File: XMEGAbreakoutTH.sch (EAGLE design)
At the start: 23 parts, among them IC1 XMEGA16A4

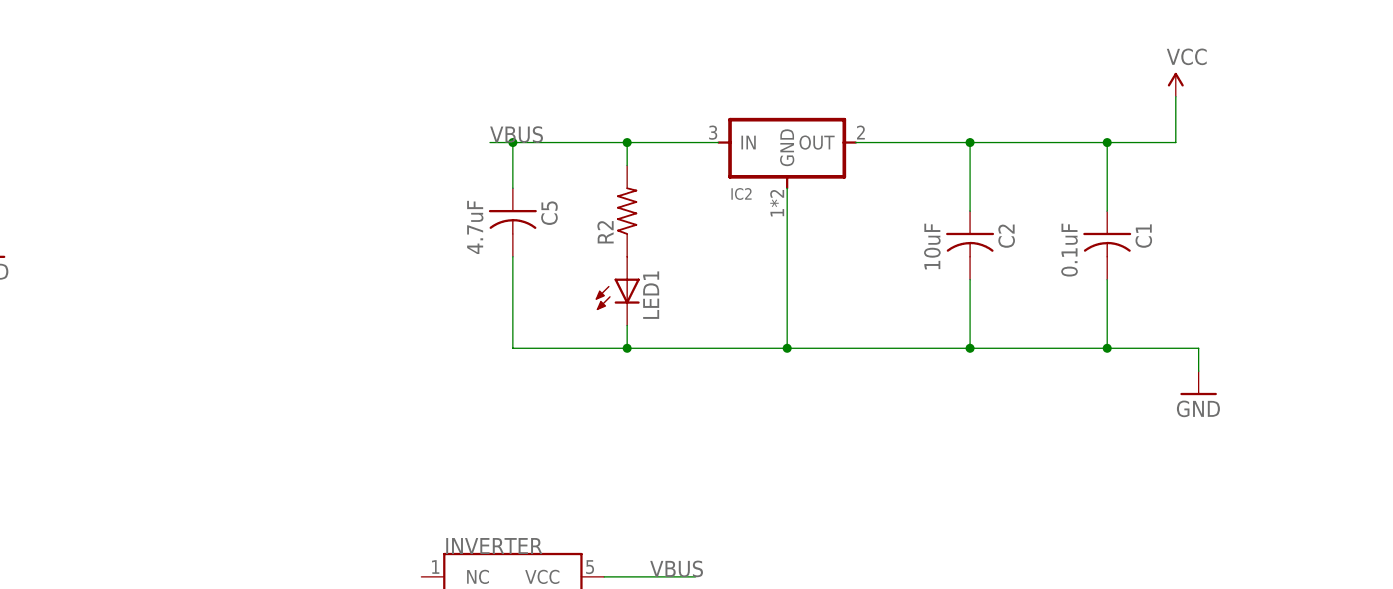
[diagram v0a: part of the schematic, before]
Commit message: caps on each port
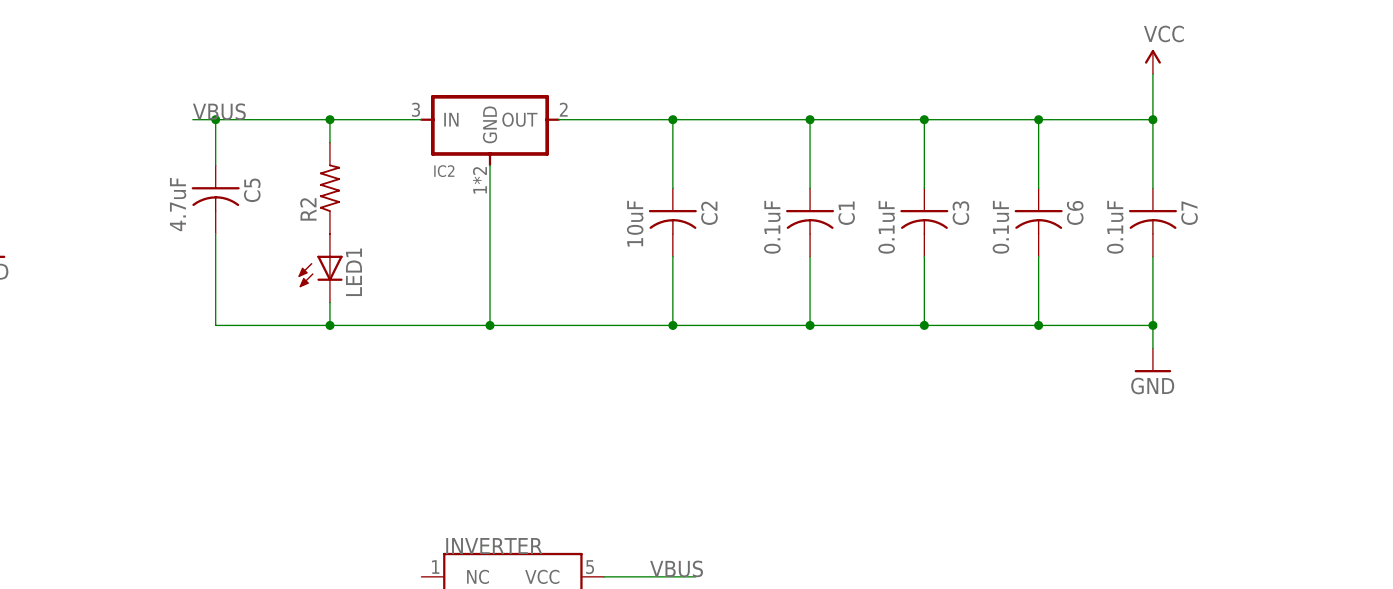
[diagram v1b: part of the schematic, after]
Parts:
- added C3: 0.1uF, fab:CAP-US1206FAB
- added C6, C7: 0.1uF, fab:CAP-US1206
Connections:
- net GND: now also C3.2, C6.2, C7.2
- net VCC: now also C3.1, C6.1, C7.1
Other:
- moved on the sheet: C1, C2, C5, IC2, LED1, R2
